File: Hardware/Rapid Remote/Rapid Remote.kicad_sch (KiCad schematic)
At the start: 4 parts

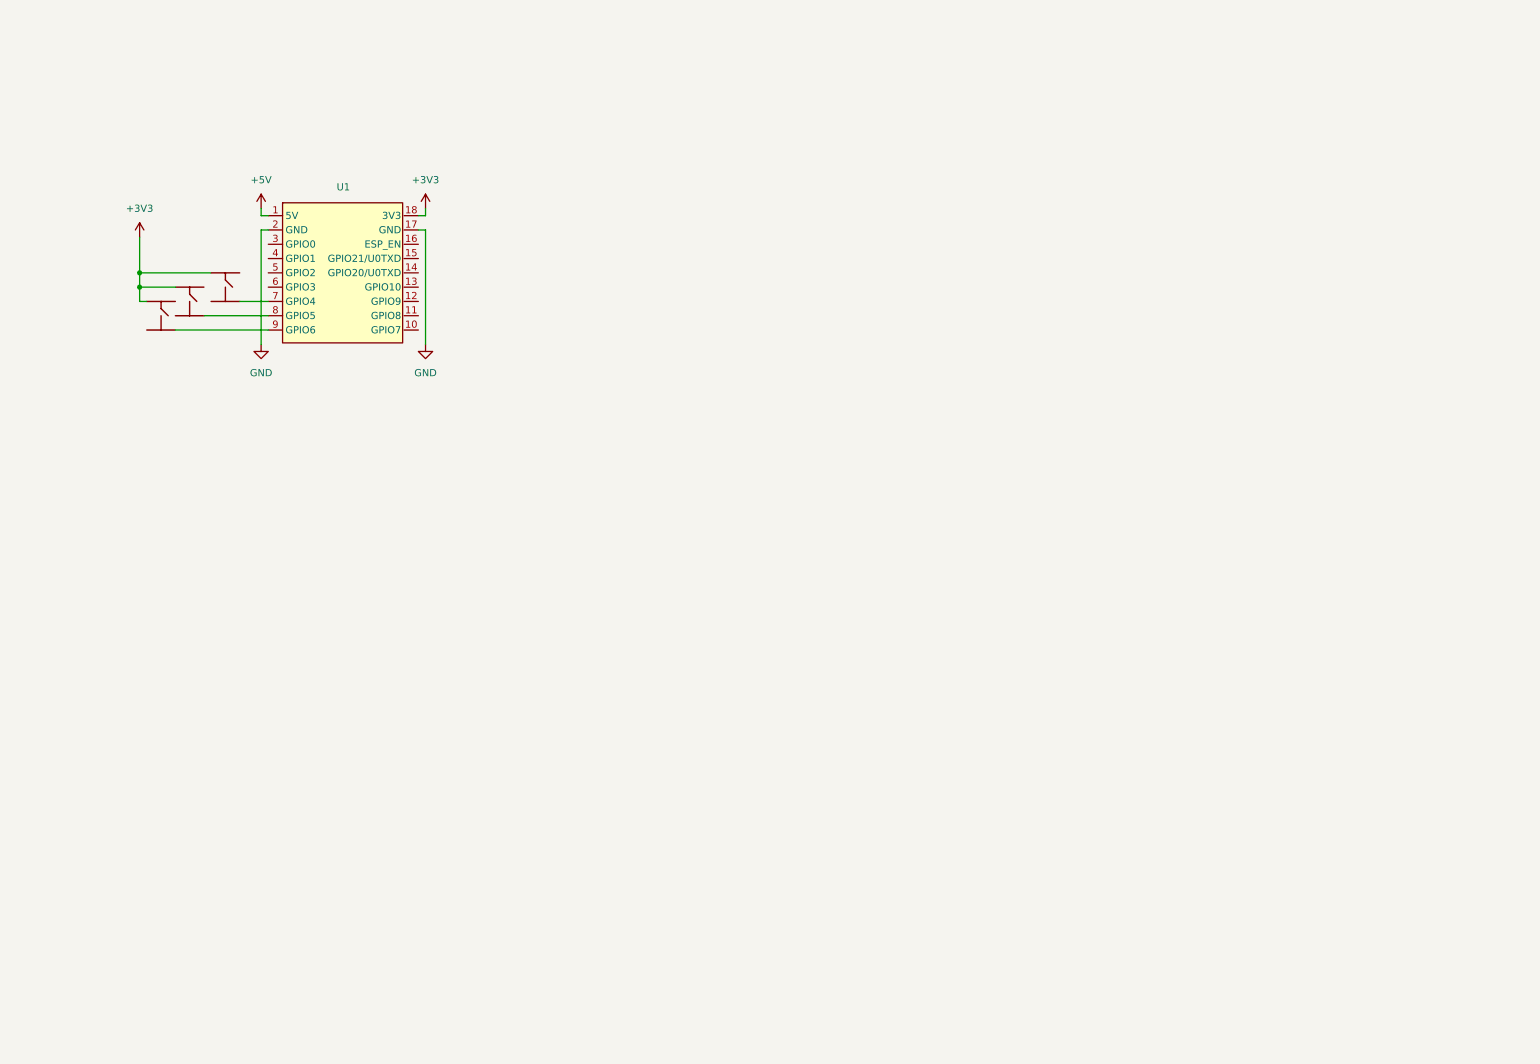
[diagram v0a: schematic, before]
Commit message: added components and schematic for rev b of the remote
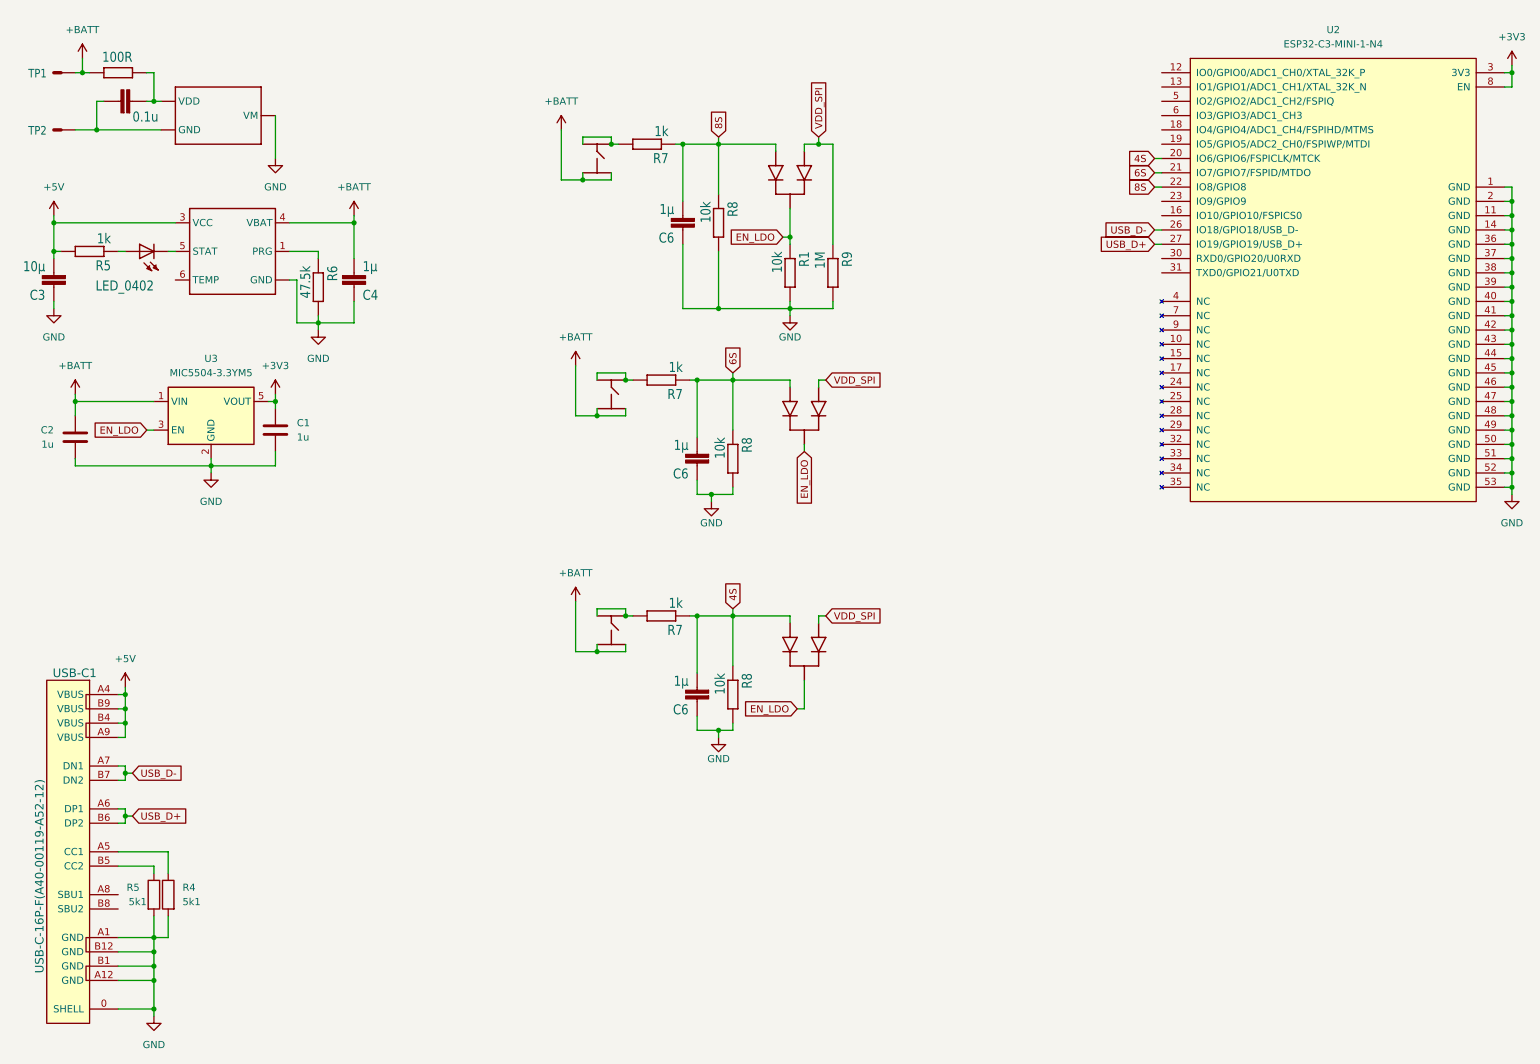
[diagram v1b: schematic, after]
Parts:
- removed U1: ~, Personal:ESP32-C3-DevKit, symbol personal2:ESP32-C3_DevKit_Rev_A
- added C1, C2: 1u, Capacitor_SMD:C_0402_1005Metric, symbol Device:C
- added C3: 10µ, Capacitor_SMD:C_0402_1005Metric, symbol picoclick_c3_v1.1-eagle-import:moekoe_rcl_C0402_S
- added C4, C6 (x3): 1µ, Capacitor_SMD:C_0402_1005Metric, symbol picoclick_c3_v1.1-eagle-import:moekoe_rcl_C0402_S
- added C7: 0.1u, Capacitor_SMD:C_0402_1005Metric, symbol picoclick_c3_v1.1-eagle-import:moekoe_C-EU-0402-WOKEEPOUT_S
- added D1 (x3): DAN222G, picoclick_c3_v1.1:SOT523, symbol picoclick_c3_v1.1-eagle-import:moekoe_discrete_DAN222
- added L2: LED_0402, LED_SMD:LED_0402_1005Metric, symbol picoclick_c3_v1.1-eagle-import:moekoe_led_LED_0402
- added R1, R8 (x3): 10k, Resistor_SMD:R_0402_1005Metric, symbol picoclick_c3_v1.1-eagle-import:moekoe_rcl_R0402
- added R10: 100R, Resistor_SMD:R_0402_1005Metric, symbol picoclick_c3_v1.1-eagle-import:moekoe_R-EU-0402-WOKEEPOUT
- added R4, R5: 5k1, Resistor_SMD:R_0402_1005Metric, symbol Device:R
- added R5, R7 (x3): 1k, Resistor_SMD:R_0402_1005Metric, symbol picoclick_c3_v1.1-eagle-import:moekoe_rcl_R0402
- added R6: 47.5k, Resistor_SMD:R_0402_1005Metric, symbol picoclick_c3_v1.1-eagle-import:moekoe_rcl_R0402
- added R9: 1M, Resistor_SMD:R_0402_1005Metric, symbol picoclick_c3_v1.1-eagle-import:moekoe_rcl_R0402
- added TP1, TP2: TP/SP-1.5X2.0, picoclick_c3_v1.1:SOLDERPAD_1.5X2.0, symbol picoclick_c3_v1.1-eagle-import:iml_elc_TP/SP-1.5X2.0
- added U2: ESP32-C3-MINI-1-N4, Personal:ESP32-­C3-­MINI­-1, symbol personal2:ESP32-­C3-­MINI­-1
- added U3: WS4518D, picoclick_c3_v1.1:DFN-6, symbol picoclick_c3_v1.1-eagle-import:moekoe_ics_WS4518D
- added U3: MIC5504-3.3YM5, Package_TO_SOT_SMD:SOT-23-5, symbol Regulator_Linear:MIC5504-3.3YM5
- added U6: XB6042I2SV, picoclick_c3_v1.1:TDFN4, symbol picoclick_c3_v1.1-eagle-import:moekoe_XB6042I2SV
- added USB-C1: USB-C-16P-F(A40-00119-A52-12), Personal:USB2.0_TYPE-C(A40-00119-A52-12), symbol personal2:USB2.0_TYPE-C(A40-00119-A52-12)
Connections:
- net +3V3: now also C1.1, U2.3 (3V3), U2.8 (EN), U3.5 (VOUT); no longer s4.P1 (1), s6.P1 (1), s8.P1 (1)
- net +5V: now also C3.P$2 (2), R5.2, U3.3 (VCC), USB-C1.A4 (VBUS), USB-C1.A9 (VBUS), USB-C1.B4 (VBUS), USB-C1.B9 (VBUS)
- net GND: now also C1.2, C2.2, C3.P$1 (1), C4.P$1 (1), C6.P$1 (1), C6.P$1 (1), C6.P$1 (1), R1.2, R4.2, R5.2, R6.2, R8.2, R8.2, R8.2, R9.2, U2.1 (GND), U2.11 (GND), U2.14 (GND), U2.2 (GND), U2.36 (GND), U2.37 (GND), U2.38 (GND), U2.39 (GND), U2.40 (GND), U2.41 (GND), U2.42 (GND), U2.43 (GND), U2.44 (GND), U2.45 (GND), U2.46 (GND), U2.47 (GND), U2.48 (GND), U2.49 (GND), U2.50 (GND), U2.51 (GND), U2.52 (GND), U2.53 (GND), U3.2 (GND), U3.2 (GND), U3.EXP (GND), U6.P4 (VM), USB-C1.0 (SHELL), USB-C1.A1 (GND), USB-C1.A12 (GND), USB-C1.B1 (GND), USB-C1.B12 (GND)
- net at s6.P2 (2): now also s6.P1 (1), R7.2
- net +BATT: now reaches s6.P3 (3)
- net +BATT: now also s4.P3 (3), s4.P4 (4), s6.P4 (4), s8.P3 (3), s8.P4 (4), C2.1, C4.P$2 (2), R10.2, TP1.1 (S), U3.1 (VIN), U3.4 (VBAT)
- net at s4.P2 (2): now also s4.P1 (1), R7.2
- net at s8.P2 (2): now also s8.P1 (1), R7.2
- new net: R4.1, USB-C1.A5 (CC1)
- new net: C7.P$2 (2), R10.1, U6.P1 (VDD)
- new net: C7.P$1 (1), TP2.1 (S), U6.EXP (GND), U6.P2 (GND), U6.P3 (GND)
- new net: R5.1, USB-C1.B5 (CC2)
- new net: R6.1, U3.1 (PRG)
- new net: L2.P$1 (C), U3.5 (STAT)
- new net: L2.P$2 (A), R5.1
- new net 4S: C6.P$2 (2), D1.2, R7.1, R8.1, U2.20 (IO6/GPIO6/FSPICLK/MTCK)
- new net 6S: C6.P$2 (2), D1.2, R7.1, R8.1, U2.21 (IO7/GPIO7/FSPID/MTDO)
- new net 8S: C6.P$2 (2), D1.2, R7.1, R8.1, U2.22 (IO8/GPIO8)
- new net EN_LDO: D1.3, D1.3, D1.3, R1.1, U3.3 (EN)
- new net USB_D+: U2.27 (IO19/GPIO19/USB_D+), USB-C1.A6 (DP1), USB-C1.B6 (DP2)
- new net USB_D-: U2.26 (IO18/GPIO18/USB_D-), USB-C1.A7 (DN1), USB-C1.B7 (DN2)
- new net VDD_SPI: D1.1, D1.1, D1.1, R9.1
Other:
- company: (none) -> Thomas Whyte-Venables
- title: (none) -> Rapid Remote

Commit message: changed latching circuit
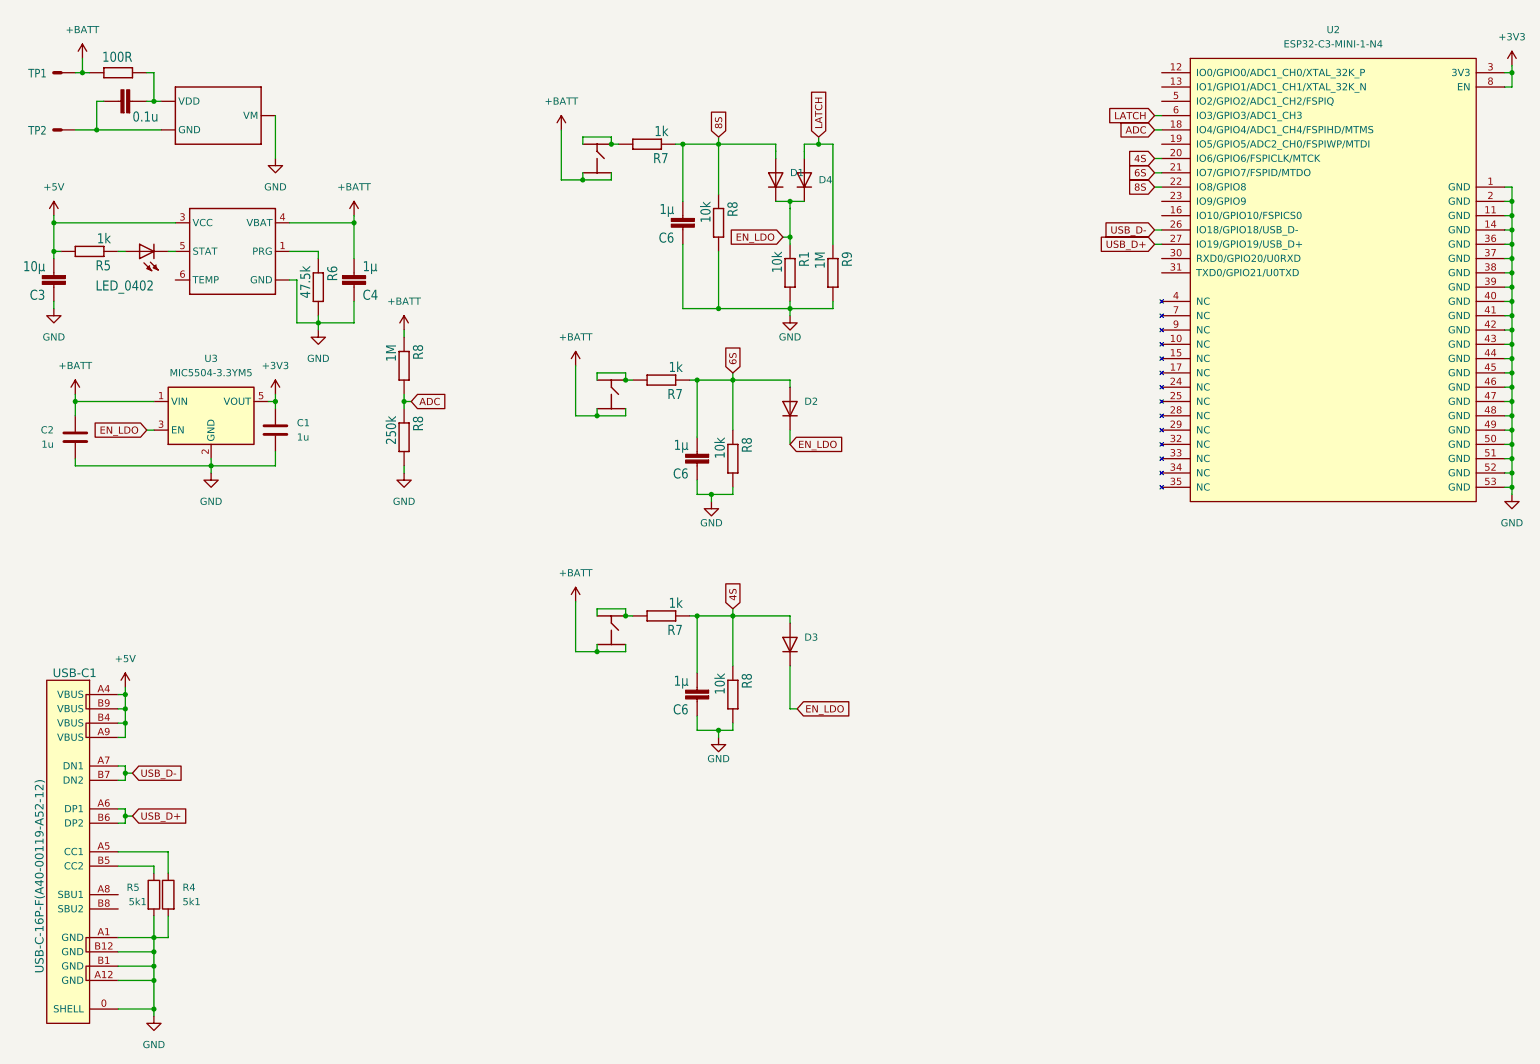
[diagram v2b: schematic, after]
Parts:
- removed D1 (x3): DAN222G, picoclick_c3_v1.1:SOT523, symbol picoclick_c3_v1.1-eagle-import:moekoe_discrete_DAN222
- added D1, D2, D3, D4: 1N4148WT, Diode_SMD:D_SOD-523, symbol Diode:1N4148WT
- added R8: 250k, Resistor_SMD:R_0402_1005Metric, symbol picoclick_c3_v1.1-eagle-import:moekoe_rcl_R0402
- added R8: 1M, Resistor_SMD:R_0402_1005Metric, symbol picoclick_c3_v1.1-eagle-import:moekoe_rcl_R0402
- TP1, TP2: footprint picoclick_c3_v1.1:SOLDERPAD_1.5X2.0 -> Personal:SOLDERPAD_1.5X2.0
- U3: footprint picoclick_c3_v1.1:DFN-6 -> Personal:DFN-6
- U6: footprint picoclick_c3_v1.1:TDFN4 -> Personal:TDFN4
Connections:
- net VDD_SPI is gone; now on net LATCH: R9.1
- net +BATT: now also R8.1
- net 4S: now also D3.2 (A)
- net 6S: now also D2.2 (A)
- net 8S: now also D1.2 (A)
- net EN_LDO: now also D1.1 (K), D2.1 (K), D3.1 (K), D4.1 (K)
- net GND: now also R8.2
- net ADC: now reaches U2.18 (IO4/GPIO4/ADC1_CH4/FSPIHD/MTMS)
- net ADC: now also R8.1, R8.2
- net LATCH: now reaches U2.6 (IO3/GPIO3/ADC1_CH3)
- net LATCH: now also D4.2 (A)

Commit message: added initial remote code and more layout for remote
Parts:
- removed C3: 10µ, Capacitor_SMD:C_0402_1005Metric, symbol picoclick_c3_v1.1-eagle-import:moekoe_rcl_C0402_S
- removed C4, C6 (x3): 1µ, Capacitor_SMD:C_0402_1005Metric, symbol picoclick_c3_v1.1-eagle-import:moekoe_rcl_C0402_S
- removed C7: 0.1u, Capacitor_SMD:C_0402_1005Metric, symbol picoclick_c3_v1.1-eagle-import:moekoe_C-EU-0402-WOKEEPOUT_S
- removed L2: LED_0402, LED_SMD:LED_0402_1005Metric, symbol picoclick_c3_v1.1-eagle-import:moekoe_led_LED_0402
- removed R10: 100R, Resistor_SMD:R_0402_1005Metric, symbol picoclick_c3_v1.1-eagle-import:moekoe_R-EU-0402-WOKEEPOUT
- added C3: 0.1u, Capacitor_SMD:C_0402_1005Metric, symbol Device:C
- added C4: 10u, Capacitor_SMD:C_0402_1005Metric, symbol Device:C
- added C5, C6, C7, C8: 1u, Capacitor_SMD:C_0402_1005Metric, symbol Device:C
- added D5: LED, LED_SMD:LED_0402_1005Metric, symbol Device:LED
- added R7: 100R, Resistor_SMD:R_0402_1005Metric, symbol picoclick_c3_v1.1-eagle-import:moekoe_rcl_R0402
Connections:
- net +5V: now also C4.1
- net +BATT: now also C5.1, R7.2
- net 4S: now also C8.1
- net 6S: now also C7.1
- net 8S: now also C6.1
- net GND: now also C4.2, C5.2, C6.2, C7.2, C8.2
- net at U6.P1 (VDD): now also C3.2, R7.1
- net at TP2.1 (S), U6.EXP (GND), U6.P2 (GND)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: now also C3.1
- net at U3.5 (STAT): now also D5.1 (K)
- net at R5.1: now also D5.2 (A)
